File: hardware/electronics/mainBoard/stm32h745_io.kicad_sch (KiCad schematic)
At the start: 8 parts, among them SW1 VAL, SW2 VAL, U1 STM32H745ZIT6

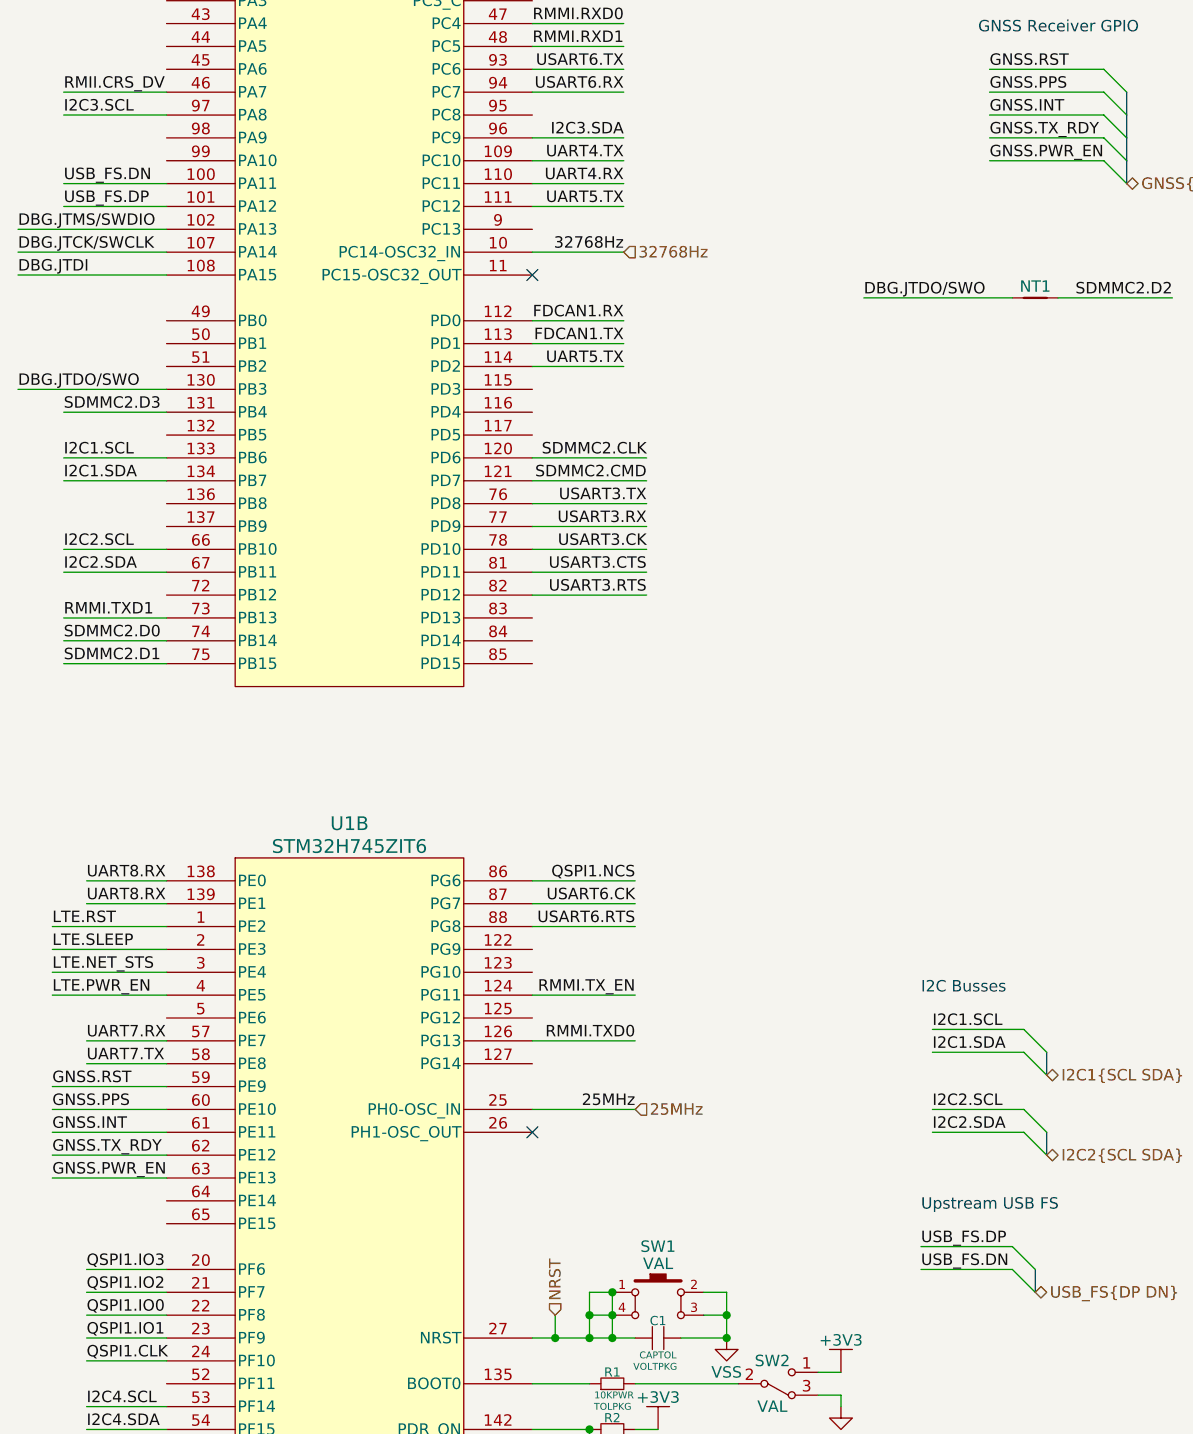
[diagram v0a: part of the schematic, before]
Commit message: renamed USB net
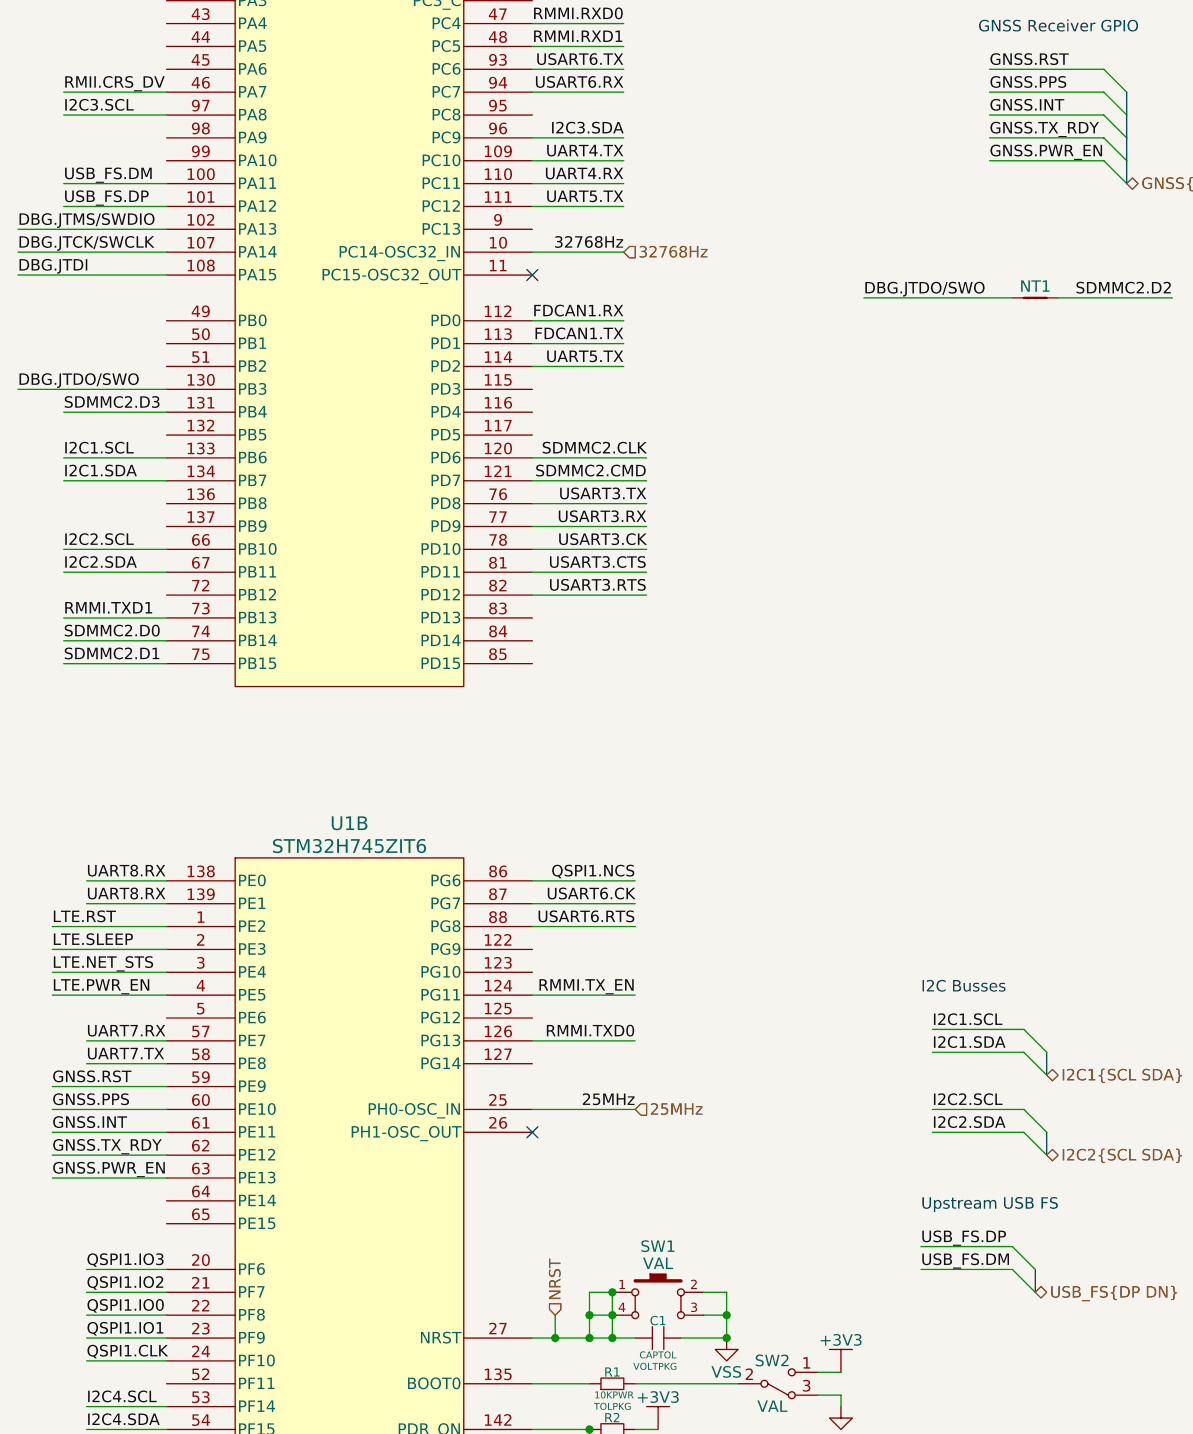
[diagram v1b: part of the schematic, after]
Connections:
- net USB_FS.DN renamed USB_FS.DM
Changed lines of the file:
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@@
 		)
 	)
-	(label "USB_FS.DN"
+	(label "USB_FS.DM"
 		(at 31.75 50.8 0)
 		(effects
@@
 		)
 	)
-	(label "USB_FS.DN"
+	(label "USB_FS.DM"
 		(at 127 171.45 0)
 		(effects

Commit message: added IO
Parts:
- C1: symbol DS-Passives:C_horizontal -> lib_sch:C_horizontal
- NT1: symbol Device:NetTie_2 -> lib_sch:NetTie_2
- R1, R2, R3: symbol DS-Passives:R_horizontal -> lib_sch:R_horizontal
- SW1: symbol DS-Switches:SPST-NO Button -> lib_sch:SPST-NO Button
- SW2: symbol DS-Switches:SPDT -> lib_sch:SPDT
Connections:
- net LTE.PWR_EN: now also U1.5 (PE6); no longer U1.4 (PE5)
- net NRST: now also SW1.2; no longer SW1.4
- net VSS: now also SW1.4; no longer SW1.2
- new net LTE.MOD_STS: U1.4 (PE5)
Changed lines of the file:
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@@
 	)
 	(bus_entry
+		(at 147.32 24.13)
+		(size 2.54 2.54)
+		(stroke
+			(width 0)
+			(type default)
+		)
+	)
+	(bus_entry
 		(at 170.18 147.32)
 		(size 2.54 2.54)
@@
 	)
 	(bus_entry
-		(at 147.32 24.13)
+		(at 147.32 26.67)
 		(size 2.54 2.54)
 		(stroke
@@
 	(wire
 		(pts
+			(xy 30.48 143.51) (xy 43.18 143.51)
+		)
+		(stroke
+			(width 0)
+			(type default)
+		)
+	)
+	(wire
+		(pts
 			(xy 189.23 77.47) (xy 205.74 77.47)
 		)
@@
 	(wire
 		(pts
-			(xy 30.48 140.97) (xy 43.18 140.97)
-		)
-		(stroke
-			(width 0)
-			(type default)
-		)
-	)
-	(wire
-		(pts
 			(xy 34.29 171.45) (xy 43.18 171.45)
 		)
@@
 		)
 	)
+	(wire
+		(pts
+			(xy 30.48 140.97) (xy 43.18 140.97)
+		)
+		(stroke
+			(width 0)
+			(type default)
+		)
+	)
 	(bus
 		(pts
@@
 		)
 	)
+	(wire
+		(pts
+			(xy 147.32 24.13) (xy 134.62 24.13)
+		)
+		(stroke
+			(width 0)
+			(type default)
+		)
+	)
 	(bus
 		(pts
@@
 	(wire
 		(pts
-			(xy 134.62 24.13) (xy 147.32 24.13)
+			(xy 134.62 26.67) (xy 147.32 26.67)
 		)
 		(stroke
@@
 		)
 	)
+	(bus
+		(pts
+			(xy 149.86 26.67) (xy 149.86 29.21)
+		)
+		(stroke
+			(width 0)
+			(type default)
+		)
+	)
 	(wire
 		(pts
@@
 		)
 	)
+	(label "LTE.PWR_EN"
+		(at 30.48 143.51 0)
+		(effects
+			(font
+				(size 1.27 1.27)
+			)
+			(justify left bottom)
+		)
+	)
 	(label "USART6.CK"
 		(at 220.98 125.73 0)
@@
 		)
 	)
-	(label "LTE.PWR_EN"
-		(at 30.48 140.97 0)
-		(effects
-			(font
-				(size 1.27 1.27)
-			)
-			(justify left bottom)
-		)
-	)
 	(label "25MHz"
 		(at 95.25 153.67 180)
@@
 	)
 	(label "LTE.PWR_EN"
-		(at 134.62 24.13 0)
+		(at 134.62 26.67 0)
 		(effects
 			(font
@@
 		)
 	)
+	(label "LTE.MOD_STS"
+		(at 30.48 140.97 0)
+		(effects
+			(font
+				(size 1.27 1.27)
+			)
+			(justify left bottom)
+		)
+	)
 	(label "QSPI1.IO3"
 		(at 189.23 102.87 0)
@@
 		)
 	)
+	(label "LTE.MOD_STS"
+		(at 134.62 24.13 0)
+		(effects
+			(font
+				(size 1.27 1.27)
+			)
+			(justify left bottom)
+		)
+	)
 	(label "USART6.RX"
 		(at 93.98 40.64 180)
@@
 	(hierarchical_label "LTE{RST SLEEP NET_STS PWR_EN}"
 		(shape bidirectional)
-		(at 149.86 26.67 0)
+		(at 149.86 29.21 0)
 		(effects
 			(font
@@
 	)
 	(symbol
-		(lib_id "DS-Power:VSS")
+		(lib_id "lib_sch:VSS")
 		(at 105.41 179.07 0)
 		(unit 1)
@@
 	)
 	(symbol
-		(lib_id "DS-Power:VSS")
+		(lib_id "lib_sch:VSS")
 		(at 97.79 195.58 0)
 		(unit 1)
@@
 	)
 	(symbol
-		(lib_id "DS-Power:+3V3")
+		(lib_id "lib_sch:+3V3")
 		(at 118.11 182.88 0)
 		(unit 1)
@@
 	)
 	(symbol
-		(lib_id "Device:NetTie_2")
+		(lib_id "lib_sch:NetTie_2")
 		(at 139.7 63.5 0)
 		(unit 1)
@@
 	)
 	(symbol
-		(lib_id "DS-Power:VSS")
+		(lib_id "lib_sch:VSS")
 		(at 118.11 186.69 0)
 		(unit 1)
@@
 	)
 	(symbol
-		(lib_id "DS-Passives:R_horizontal")
+		(lib_id "lib_sch:R_horizontal")
 		(at 92.71 189.23 0)
 		(unit 1)
@@
 	)
 	(symbol
-		(lib_id "DS-Power:+3V3")
+		(lib_id "lib_sch:+3V3")
 		(at 97.79 189.23 0)
 		(unit 1)
@@
 	)
 	(symbol
-		(lib_id "DS-Switches:SPDT")
+		(lib_id "lib_sch:SPDT")
 		(at 110.49 184.15 0)
 		(unit 1)
@@
 	)
 	(symbol
-		(lib_id "DS-Passives:R_horizontal")
+		(lib_id "lib_sch:R_horizontal")
 		(at 92.71 194.31 0)
 		(unit 1)
@@
 	)
 	(symbol
-		(lib_id "DS-Passives:R_horizontal")
+		(lib_id "lib_sch:R_horizontal")
 		(at 92.71 184.15 0)
 		(unit 1)
@@
 	)
 	(symbol
-		(lib_id "DS-Switches:SPST-NO Button")
+		(lib_id "lib_sch:SPST-NO Button")
 		(at 97.79 175.26 0)
 		(unit 1)
@@
 	)
 	(symbol
-		(lib_id "DS-Passives:C_horizontal")
+		(lib_id "lib_sch:C_horizontal")
 		(at 97.79 179.07 0)
 		(unit 1)
